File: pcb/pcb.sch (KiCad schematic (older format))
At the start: 99 parts, among them SW1 SW_Push, SW10 SW_Push, SW11 SW_Push, SW12 SW_Push, SW13 SW_Push, SW14 SW_Push, SW15 SW_Push, SW16 SW_Push, SW17 SW_Push, SW18 SW_Push, SW19 SW_Push, SW2 SW_Push, SW20 SW_Push, SW21 SW_Push, SW22 SW_Push, SW23 SW_Push, SW24 SW_Push, SW25 SW_Push, SW26 SW_Push, SW27 SW_Push, SW28 SW_Push, SW29 SW_Push, SW3 SW_Push, SW30 SW_Push, SW31 SW_Push, SW32 SW_Push, SW33 SW_Push, SW34 SW_Push, SW35 SW_Push, SW36 SW_Push, SW37 SW_Push, SW38 SW_Push, SW39 SW_Push, SW4 SW_Push, SW40 SW_Push, SW41 SW_Push, SW42 SW_Push, SW43 SW_Push, SW44 SW_Push, SW45 SW_Push, SW46 SW_Push, SW47 SW_Push, SW48 SW_Push, SW5 SW_Push, SW6 SW_Push, SW7 SW_Push, SW8 SW_Push, SW9 SW_Push, U1 ATmega32U4-AU

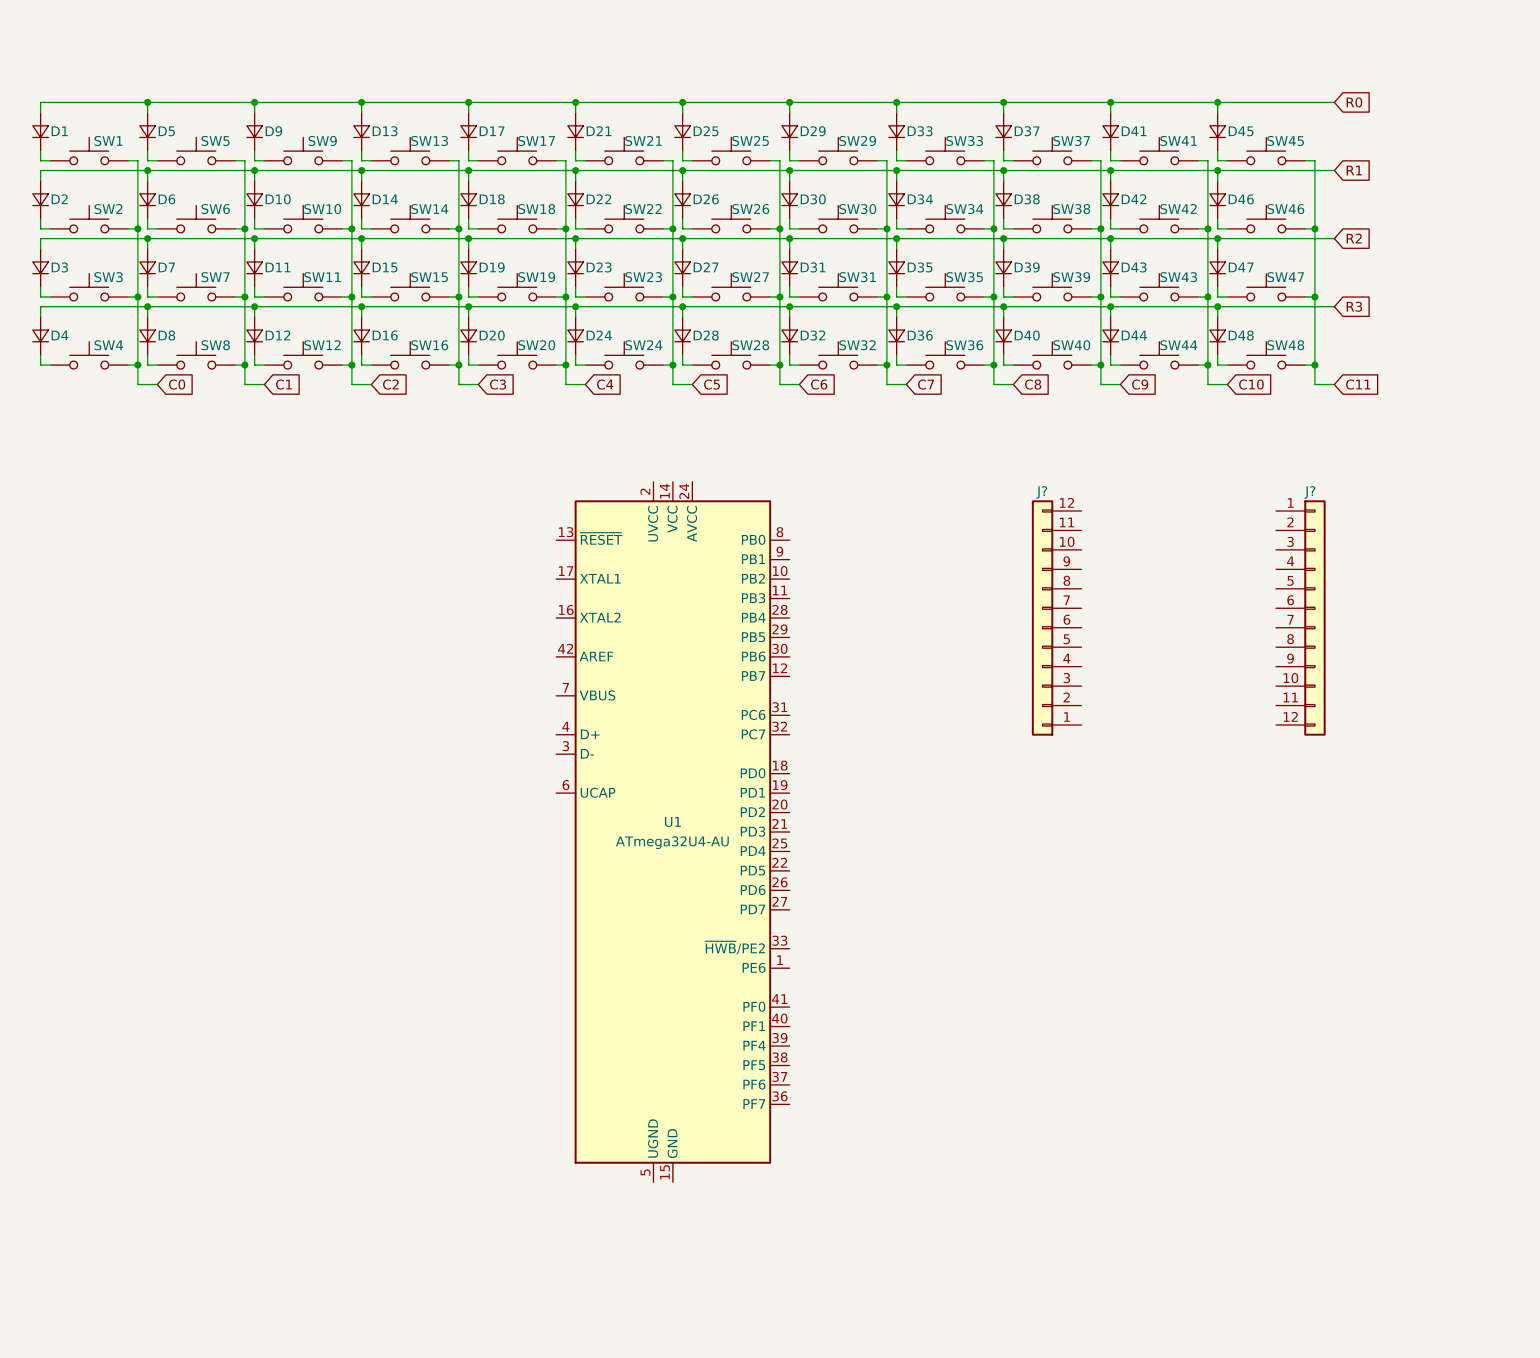
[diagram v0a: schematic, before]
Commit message: add crystal, usb connector
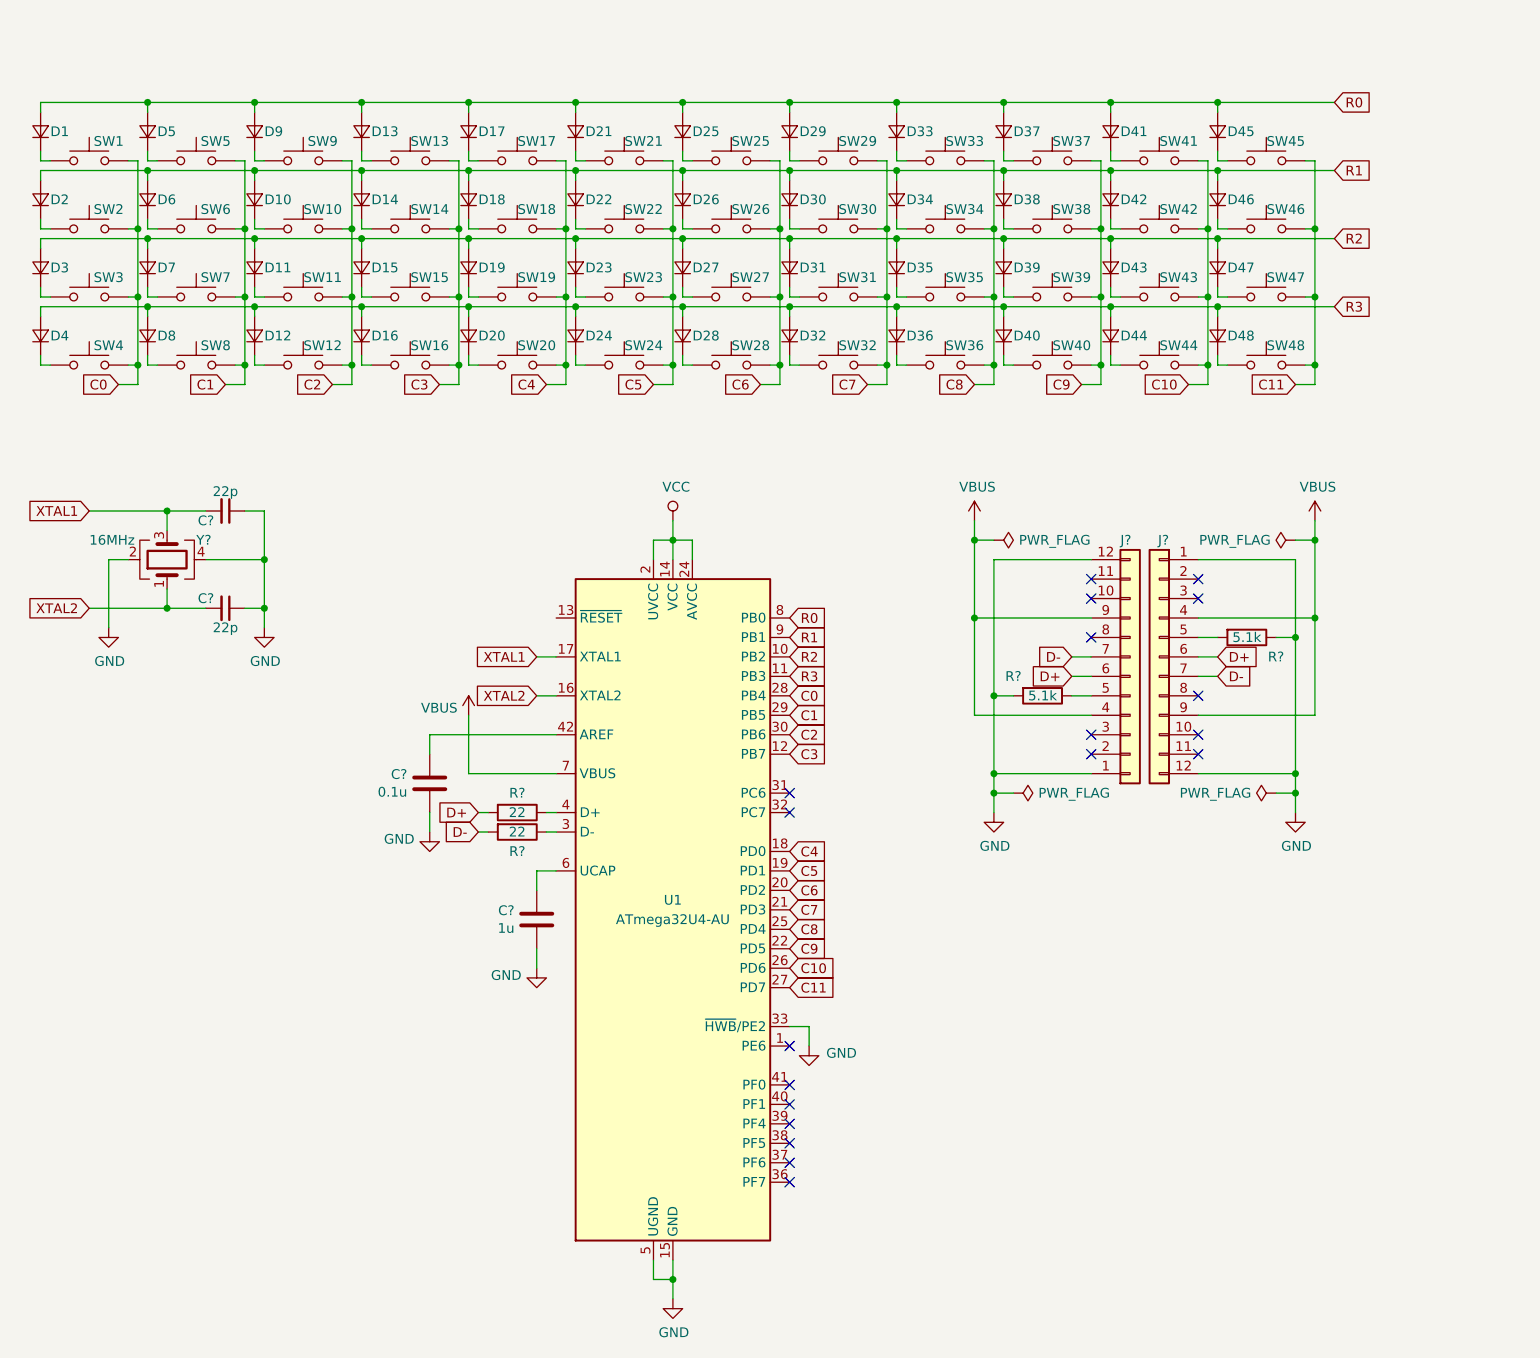
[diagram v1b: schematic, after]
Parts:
- removed J? (x2): Conn_01x12, symbol Connector_Generic:Conn_01x12
- added C? (x2): 22p, symbol Device:C_Small
- added C?: 0.1u, symbol Device:C
- added C?: 1u, symbol Device:C
- added J? (x2): Conn_01x12, symbol Connector_Generic:Conn_01x12
- added R? (x2): 22, symbol Device:R
- added R? (x2): 5.1k, symbol Device:R
- added Y?: 16MHz, symbol Device:Crystal_GND24
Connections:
- net C0: now also U1.28 (PB4)
- net C1: now also U1.29 (PB5)
- net C10: now also U1.26 (PD6)
- net C11: now also U1.27 (PD7)
- net C2: now also U1.30 (PB6)
- net C3: now also U1.12 (PB7)
- net C4: now also U1.18 (PD0)
- net C5: now also U1.19 (PD1)
- net C6: now also U1.20 (PD2)
- net C7: now also U1.21 (PD3)
- net C8: now also U1.25 (PD4)
- net C9: now also U1.22 (PD5)
- net R0: now also U1.8 (PB0)
- net R1: now also U1.9 (PB1)
- net R2: now also U1.10 (PB2)
- net R3: now also U1.11 (PB3)
- net VCC: now reaches U1.14 (VCC), U1.34 (VCC)
- net VCC: now also U1.2 (UVCC), U1.24 (AVCC), U1.44 (AVCC)
- net GND: now reaches U1.15 (GND), U1.23 (GND), U1.35 (GND), U1.43 (GND)
- net GND: now also U1.33 (~HWB~/PE2), U1.5 (UGND), C?.1, C?.1, C?.2, C?.2, J?.1 (Pin_1), J?.1 (Pin_1), J?.12 (Pin_12), J?.12 (Pin_12), R?.1, R?.2, Y?.2, Y?.4
- net XTAL2: now reaches U1.16 (XTAL2)
- net XTAL2: now also C?.2, Y?.1
- net XTAL1: now reaches U1.17 (XTAL1)
- net XTAL1: now also C?.2, Y?.3
- net at U1.3 (D-): now also R?.1
- net at U1.4 (D+): now also R?.1
- net at U1.42 (AREF): now also C?.1
- net at U1.6 (UCAP): now also C?.1
- net VBUS: now reaches U1.7 (VBUS)
- net VBUS: now also J?.4 (Pin_4), J?.4 (Pin_4), J?.9 (Pin_9), J?.9 (Pin_9)
- new net: J?.5 (Pin_5), R?.1
- new net: J?.5 (Pin_5), R?.2
- new net D+: J?.6 (Pin_6), J?.6 (Pin_6), R?.2
- new net D-: J?.7 (Pin_7), J?.7 (Pin_7), R?.2
- no-connect marks 0 -> 19
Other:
- moved on the sheet: U1

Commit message: add schematics
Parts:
- removed J? (x2): Conn_01x12, symbol Connector_Generic:Conn_01x12
- removed R? (x2): 5.1k, symbol Device:R
- added C? (x4): 0.1u, symbol Device:C_Small
- added C?: 4.7u, symbol Device:C_Small
- added J?: USB_C_Receptacle_USB2.0, symbol Connector:USB_C_Receptacle_USB2.0
- added R? (x2): 5.1k, symbol Device:R
- added R? (x2): 22, symbol Device:R
- added R?: 10k, symbol Device:R
- added SW?: SW_Push, symbol Switch:SW_Push
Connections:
- net D+: now also R?.1
- net D-: now also R?.1
- net GND: now also C?.2, C?.2, C?.2, C?.2, C?.2, J?.A1 (GND), J?.A12 (GND), J?.B1 (GND), J?.B12 (GND), J?.S1 (SHIELD), R?.1, R?.1, SW?.2
- net VBUS: now also J?.A4 (VBUS), J?.A9 (VBUS), J?.B4 (VBUS), J?.B9 (VBUS)
- net VCC: now also C?.1, C?.1, C?.1, C?.1, C?.1, R?.1
- net RESET: now reaches U1.13 (~RESET)
- net RESET: now also R?.2, SW?.1
- new net: J?.A5 (CC1), R?.2
- new net: J?.A6 (D+), J?.B6 (D+), R?.2
- new net: J?.A7 (D-), J?.B7 (D-), R?.2
- new net: J?.B5 (CC2), R?.2
- no-connect marks 19 -> 11
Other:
- moved on the sheet: C?, Y?

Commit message: add components
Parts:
- C1, C2, C3, C4, C5, C6, C7, C8, C9: renamed from C?; footprint (none) -> Capacitor_SMD:C_1206_3216Metric_Pad1.42x1.75mm_HandSolder
- D1, D48: footprint (none) -> Diode_SMD:D_SOD-123F
- D10: renamed from D37; footprint (none) -> Diode_SMD:D_SOD-123F
- D11: renamed from D41; footprint (none) -> Diode_SMD:D_SOD-123F
- D12: renamed from D45; footprint (none) -> Diode_SMD:D_SOD-123F
- D13: renamed from D2; footprint (none) -> Diode_SMD:D_SOD-123F
- D14: renamed from D6; footprint (none) -> Diode_SMD:D_SOD-123F
- D15: renamed from D10; footprint (none) -> Diode_SMD:D_SOD-123F
- D16: renamed from D14; footprint (none) -> Diode_SMD:D_SOD-123F
- D17: renamed from D18; footprint (none) -> Diode_SMD:D_SOD-123F
- D18: renamed from D22; footprint (none) -> Diode_SMD:D_SOD-123F
- D19: renamed from D26; footprint (none) -> Diode_SMD:D_SOD-123F
- D2: renamed from D5; footprint (none) -> Diode_SMD:D_SOD-123F
- D20: renamed from D30; footprint (none) -> Diode_SMD:D_SOD-123F
- D21: renamed from D34; footprint (none) -> Diode_SMD:D_SOD-123F
- D22: renamed from D38; footprint (none) -> Diode_SMD:D_SOD-123F
- D23: renamed from D42; footprint (none) -> Diode_SMD:D_SOD-123F
- D24: renamed from D46; footprint (none) -> Diode_SMD:D_SOD-123F
- D25: renamed from D3; footprint (none) -> Diode_SMD:D_SOD-123F
- D26: renamed from D7; footprint (none) -> Diode_SMD:D_SOD-123F
- D27: renamed from D11; footprint (none) -> Diode_SMD:D_SOD-123F
- D28: renamed from D15; footprint (none) -> Diode_SMD:D_SOD-123F
- D29: renamed from D19; footprint (none) -> Diode_SMD:D_SOD-123F
- D3: renamed from D9; footprint (none) -> Diode_SMD:D_SOD-123F
- D30: renamed from D23; footprint (none) -> Diode_SMD:D_SOD-123F
- D31: renamed from D27; footprint (none) -> Diode_SMD:D_SOD-123F
- D32: renamed from D31; footprint (none) -> Diode_SMD:D_SOD-123F
- D33: renamed from D35; footprint (none) -> Diode_SMD:D_SOD-123F
- D34: renamed from D39; footprint (none) -> Diode_SMD:D_SOD-123F
- D35: renamed from D43; footprint (none) -> Diode_SMD:D_SOD-123F
- D36: renamed from D47; footprint (none) -> Diode_SMD:D_SOD-123F
- D37: renamed from D4; footprint (none) -> Diode_SMD:D_SOD-123F
- D38: renamed from D8; footprint (none) -> Diode_SMD:D_SOD-123F
- D39: renamed from D12; footprint (none) -> Diode_SMD:D_SOD-123F
- D4: renamed from D13; footprint (none) -> Diode_SMD:D_SOD-123F
- D40: renamed from D16; footprint (none) -> Diode_SMD:D_SOD-123F
- D41: renamed from D20; footprint (none) -> Diode_SMD:D_SOD-123F
- D42: renamed from D24; footprint (none) -> Diode_SMD:D_SOD-123F
- D43: renamed from D28; footprint (none) -> Diode_SMD:D_SOD-123F
- D44: renamed from D32; footprint (none) -> Diode_SMD:D_SOD-123F
- D45: renamed from D36; footprint (none) -> Diode_SMD:D_SOD-123F
- D46: renamed from D40; footprint (none) -> Diode_SMD:D_SOD-123F
- D47: renamed from D44; footprint (none) -> Diode_SMD:D_SOD-123F
- D5: renamed from D17; footprint (none) -> Diode_SMD:D_SOD-123F
- D6: renamed from D21; footprint (none) -> Diode_SMD:D_SOD-123F
- D7: renamed from D25; footprint (none) -> Diode_SMD:D_SOD-123F
- D8: renamed from D29; footprint (none) -> Diode_SMD:D_SOD-123F
- D9: renamed from D33; footprint (none) -> Diode_SMD:D_SOD-123F
- J1: renamed from J?; footprint (none) -> digikey-footprints:USB-C_Female_CX70M-24P1
- R1, R2, R3, R4, R5, R6, R7: renamed from R?; footprint (none) -> Resistor_SMD:R_1206_3216Metric_Pad1.42x1.75mm_HandSolder
- SW1, SW48: footprint (none) -> Keebio-Parts:MX_Plate_100H
- SW10: renamed from SW37; footprint (none) -> Keebio-Parts:MX_Plate_100H
- SW11: renamed from SW41; footprint (none) -> Keebio-Parts:MX_Plate_100H
- SW12: renamed from SW45; footprint (none) -> Keebio-Parts:MX_Plate_100H
- SW13: renamed from SW2; footprint (none) -> Keebio-Parts:MX_Plate_100H
- SW14: renamed from SW6; footprint (none) -> Keebio-Parts:MX_Plate_100H
- SW15: renamed from SW10; footprint (none) -> Keebio-Parts:MX_Plate_100H
- SW16: renamed from SW14; footprint (none) -> Keebio-Parts:MX_Plate_100H
- SW17: renamed from SW18; footprint (none) -> Keebio-Parts:MX_Plate_100H
- SW18: renamed from SW22; footprint (none) -> Keebio-Parts:MX_Plate_100H
- SW19: renamed from SW26; footprint (none) -> Keebio-Parts:MX_Plate_100H
- SW2: renamed from SW5; footprint (none) -> Keebio-Parts:MX_Plate_100H
- SW20: renamed from SW30; footprint (none) -> Keebio-Parts:MX_Plate_100H
- SW21: renamed from SW34; footprint (none) -> Keebio-Parts:MX_Plate_100H
- SW22: renamed from SW38; footprint (none) -> Keebio-Parts:MX_Plate_100H
- SW23: renamed from SW42; footprint (none) -> Keebio-Parts:MX_Plate_100H
- SW24: renamed from SW46; footprint (none) -> Keebio-Parts:MX_Plate_100H
- SW25: renamed from SW3; footprint (none) -> Keebio-Parts:MX_Plate_100H
- SW26: renamed from SW7; footprint (none) -> Keebio-Parts:MX_Plate_100H
- SW27: renamed from SW11; footprint (none) -> Keebio-Parts:MX_Plate_100H
- SW28: renamed from SW15; footprint (none) -> Keebio-Parts:MX_Plate_100H
- SW29: renamed from SW19; footprint (none) -> Keebio-Parts:MX_Plate_100H
- SW3: renamed from SW9; footprint (none) -> Keebio-Parts:MX_Plate_100H
- SW30: renamed from SW23; footprint (none) -> Keebio-Parts:MX_Plate_100H
- SW31: renamed from SW27; footprint (none) -> Keebio-Parts:MX_Plate_100H
- SW32: renamed from SW31; footprint (none) -> Keebio-Parts:MX_Plate_100H
- SW33: renamed from SW35; footprint (none) -> Keebio-Parts:MX_Plate_100H
- SW34: renamed from SW39; footprint (none) -> Keebio-Parts:MX_Plate_100H
- SW35: renamed from SW43; footprint (none) -> Keebio-Parts:MX_Plate_100H
- SW36: renamed from SW47; footprint (none) -> Keebio-Parts:MX_Plate_100H
- SW37: renamed from SW4; footprint (none) -> Keebio-Parts:MX_Plate_100H
- SW38: renamed from SW8; footprint (none) -> Keebio-Parts:MX_Plate_100H
- SW39: renamed from SW12; footprint (none) -> Keebio-Parts:MX_Plate_100H
- SW4: renamed from SW13; footprint (none) -> Keebio-Parts:MX_Plate_100H
- SW40: renamed from SW16; footprint (none) -> Keebio-Parts:MX_Plate_100H
- SW41: renamed from SW20; footprint (none) -> Keebio-Parts:MX_Plate_100H
- SW42: renamed from SW24; footprint (none) -> Keebio-Parts:MX_Plate_100H
- SW43: renamed from SW28; footprint (none) -> Keebio-Parts:MX_Plate_100H
- SW44: renamed from SW32; footprint (none) -> Keebio-Parts:MX_Plate_100H
- SW45: renamed from SW36; footprint (none) -> Keebio-Parts:MX_Plate_100H
- SW46: renamed from SW40; footprint (none) -> Keebio-Parts:MX_Plate_100H
- SW47: renamed from SW44; footprint (none) -> Keebio-Parts:MX_Plate_100H
- SW49: renamed from SW?; footprint (none) -> Button_Switch_THT:SW_PUSH_6mm_H5mm
- SW5: renamed from SW17; footprint (none) -> Keebio-Parts:MX_Plate_100H
- SW6: renamed from SW21; footprint (none) -> Keebio-Parts:MX_Plate_100H
- SW7: renamed from SW25; footprint (none) -> Keebio-Parts:MX_Plate_100H
- SW8: renamed from SW29; footprint (none) -> Keebio-Parts:MX_Plate_100H
- SW9: renamed from SW33; footprint (none) -> Keebio-Parts:MX_Plate_100H
- Y1: renamed from Y?; footprint (none) -> Crystal:Crystal_SMD_SeikoEpson_FA238-4Pin_3.2x2.5mm_HandSoldering
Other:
- moved on the sheet: J1, R1, R2, R3, R4
